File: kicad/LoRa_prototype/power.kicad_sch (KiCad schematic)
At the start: 56 parts, among them J10 SYS, J15 SYS, J2 USB_C_Receptacle_PowerOnly_6P, J3 BAT, J5 FG, J7 BQ, U1 TC1262-33, U2 BQ24074RGTT, U3 MAX17048, U4 SPV1050

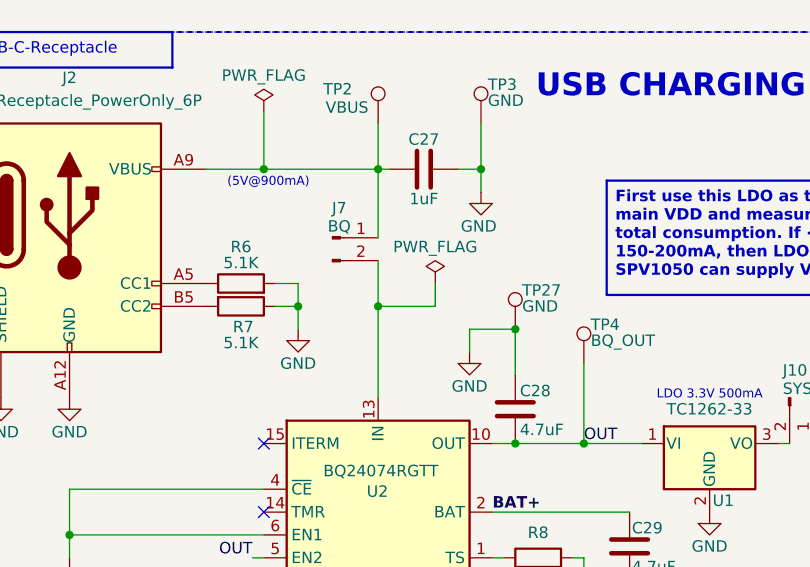
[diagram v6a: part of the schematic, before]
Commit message: Routed USB and charging IC
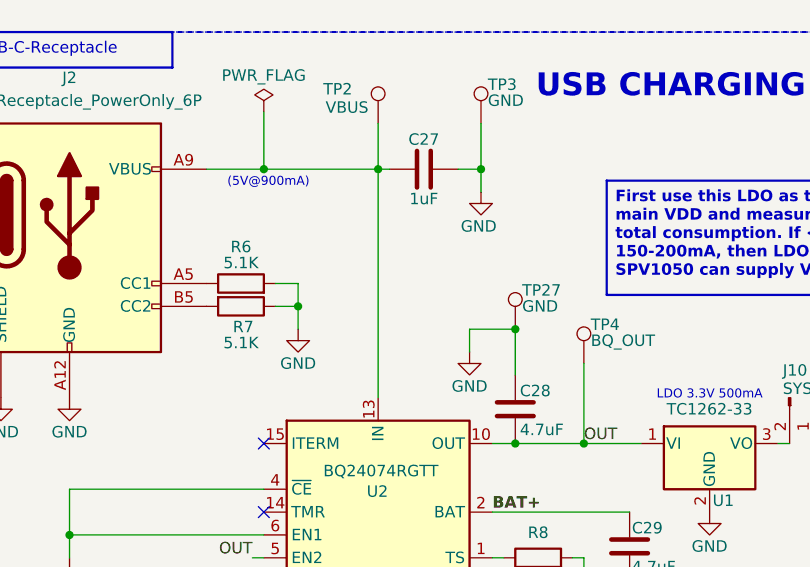
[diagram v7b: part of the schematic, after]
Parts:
- removed J7: BQ, Connector_PinHeader_2.54mm:PinHeader_1x02_P2.54mm_Vertical, symbol Connector:Conn_01x02_Pin
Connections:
- net at C27.1, J2.A9 (VBUS), J2.B9 (VBUS)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: now also U2.13 (IN)
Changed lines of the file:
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@@
 	)
 	(junction
-		(at 80.01 107.95)
-		(diameter 0)
-		(color 0 0 0 0)
-	)
-	(junction
 		(at 179.07 104.14)
 		(diameter 0)
@@
 	(wire
 		(pts
-			(xy 86.36 105.41) (xy 86.36 107.95)
-		)
-		(stroke
-			(width 0)
-			(type default)
-		)
-	)
-	(wire
-		(pts
 			(xy 128.27 123.19) (xy 133.35 123.19)
 		)
@@
 	(wire
 		(pts
-			(xy 86.36 107.95) (xy 80.01 107.95)
-		)
-		(stroke
-			(width 0)
-			(type default)
-		)
-	)
-	(wire
-		(pts
-			(xy 80.01 107.95) (xy 80.01 118.11)
-		)
-		(stroke
-			(width 0)
-			(type default)
-		)
-	)
-	(wire
-		(pts
 			(xy 153.67 123.19) (xy 153.67 125.73)
 		)
@@
 	(wire
 		(pts
-			(xy 80.01 102.87) (xy 80.01 107.95)
+			(xy 80.01 92.71) (xy 80.01 118.11)
 		)
 		(stroke
@@
 	(wire
 		(pts
-			(xy 80.01 92.71) (xy 80.01 100.33)
-		)
-		(stroke
-			(width 0)
-			(type default)
-		)
-	)
-	(wire
-		(pts
 			(xy 219.71 29.21) (xy 219.71 33.02)
 		)
@@
 	)
 	(symbol
-		(lib_id "power:PWR_FLAG")
-		(at 86.36 105.41 0)
-		(unit 1)
-		(body_style 1)
-		(exclude_from_sim no)
-		(in_bom yes)
-		(on_board yes)
-		(in_pos_files yes)
-		(dnp no)
-		(property "Reference" "#FLG010"
-			(at 86.36 103.505 0)
-			(hide yes)
-			(show_name no)
-			(do_not_autoplace no)
-			(effects
-				(font
-					(size 1.27 1.27)
-				)
-			)
-		)
-		(property "Value" "PWR_FLAG"
-			(at 86.36 101.346 0)
-			(show_name no)
-			(do_not_autoplace no)
-			(effects
-				(font
-					(size 1.27 1.27)
-				)
-			)
-		)
-		(property "Footprint" ""
-			(at 86.36 105.41 0)
-			(hide yes)
-			(show_name no)
-			(do_not_autoplace no)
-			(effects
-				(font
-					(size 1.27 1.27)
-				)
-			)
-		)
-		(property "Datasheet" ""
-			(at 86.36 105.41 0)
-			(hide yes)
-			(show_name no)
-			(do_not_autoplace no)
-			(effects
-				(font
-					(size 1.27 1.27)
-				)
-			)
-		)
-		(property "Description" "Special symbol for telling ERC where power comes from"
-			(at 86.36 105.41 0)
-			(hide yes)
-			(show_name no)
-			(do_not_autoplace no)
-			(effects
-				(font
-					(size 1.27 1.27)
-				)
-			)
-		)
-		(pin "1"
-		)
-		(instances
-			(project "LoRa_prototype"
-				(path "/9fad4700-f514-47ad-821a-b4076ecc08de/5f290f36-0c09-4232-84b9-bfe06ad06aa2"
-					(reference "#FLG010")
-					(unit 1)
-				)
-			)
-		)
-	)
-	(symbol
 		(lib_id "Device:C")
 		(at 205.74 91.44 180)
@@
 	)
 	(symbol
-		(lib_id "Connector:Conn_01x02_Pin")
-		(at 74.93 100.33 0)
-		(unit 1)
-		(body_style 1)
-		(exclude_from_sim no)
-		(in_bom yes)
-		(on_board yes)
-		(in_pos_files yes)
-		(dnp no)
-		(property "Reference" "J7"
-			(at 75.692 97.028 0)
-			(show_name no)
-			(do_not_autoplace no)
-			(effects
-				(font
-					(size 1.27 1.27)
-				)
-			)
-		)
-		(property "Value" "BQ"
-			(at 75.692 99.06 0)
-			(show_name no)
-			(do_not_autoplace no)
-			(effects
-				(font
-					(size 1.27 1.27)
-				)
-			)
-		)
-		(property "Footprint" "Connector_PinHeader_2.54mm:PinHeader_1x02_P2.54mm_Vertical"
-			(at 74.93 100.33 0)
-			(hide yes)
-			(show_name no)
-			(do_not_autoplace no)
-			(effects
-				(font
-					(size 1.27 1.27)
-				)
-			)
-		)
-		(property "Datasheet" ""
-			(at 74.93 100.33 0)
-			(hide yes)
-			(show_name no)
-			(do_not_autoplace no)
-			(effects
-				(font
-					(size 1.27 1.27)
-				)
-			)
-		)
-		(property "Description" "Generic connector, single row, 01x02, script generated"
-			(at 74.93 100.33 0)
-			(hide yes)
-			(show_name no)
-			(do_not_autoplace no)
-			(effects
-				(font
-					(size 1.27 1.27)
-				)
-			)
-		)
-		(pin "1"
-		)
-		(pin "2"
-		)
-		(instances
-			(project "LoRa_prototype"
-				(path "/9fad4700-f514-47ad-821a-b4076ecc08de/5f290f36-0c09-4232-84b9-bfe06ad06aa2"
-					(reference "J7")
-					(unit 1)
-				)
-			)
-		)
-	)
-	(symbol
 		(lib_id "power:GND")
 		(at 171.45 46.99 0)
@@
 			"15892596-2a56-42f9-87bc-d63facef6128" "15e0629a-49a6-4d89-a801-d5b90bb61a09"
 			"1606b332-549d-4356-ac60-6c5b5853a274" "17470208-3fc8-45d2-9301-407141016e98"
-			"19335232-9d4d-4c08-8b45-cce991ae32a1" "19df826f-f66b-4fd8-8010-44a60ef02bc0"
-			"1e86c9a5-56a8-443a-a601-b7e121ba0560" "2ac1fa60-a83a-486d-8e9b-da9936917350"
-			"2afca3db-305f-4098-a72a-d75c0786e537" "2c062ef6-a26b-45d0-8f0c-54ed535667b8"
-			"2f6ee398-578c-4367-b463-9ac0528bcf5e" "313899bc-2ad0-430e-8220-9b4901628631"
-			"36e6f0b5-4463-4bbd-a5eb-ef140118b323" "375cd1dd-6071-460e-b853-b380b78d5270"
+			"19df826f-f66b-4fd8-8010-44a60ef02bc0" "1e86c9a5-56a8-443a-a601-b7e121ba0560"
+			"2ac1fa60-a83a-486d-8e9b-da9936917350" "2afca3db-305f-4098-a72a-d75c0786e537"
+			"2c062ef6-a26b-45d0-8f0c-54ed535667b8" "2f6ee398-578c-4367-b463-9ac0528bcf5e"
+			"313899bc-2ad0-430e-8220-9b4901628631" "375cd1dd-6071-460e-b853-b380b78d5270"
 			"3869c621-7daa-4418-8ebe-a4226664ba23" "3b55cd7b-7118-4a57-bd28-a414f04beafe"
 			"3b7a4b9a-dfea-4b2d-ba0f-ee9f8ddfd35f" "3b7d618b-25e5-4183-ac75-f4e0437d3862"
@@
 			"6445f31d-8eb7-40e8-bbb4-238bfed47718" "66c26107-e4c7-45bf-802c-2413609b436a"
 			"6ac0af04-d7a4-4950-bed7-f84b7f1c962d" "6afd0259-80ed-4b22-b43b-e3c8370e289e"
-			"6c4368cd-6a92-4c4c-9005-fe4d29829b70" "6d50a834-2d9b-4ec7-a673-4275efa85f1e"
-			"6e0891ad-1c62-48af-ac2e-4c1d928da482" "6eb8ca3a-7038-41fb-86b1-b4cb45f65892"
+			"6c4368cd-6a92-4c4c-9005-fe4d29829b70" "6eb8ca3a-7038-41fb-86b1-b4cb45f65892"
 			"7542a80e-1430-4bb9-bab3-85b6fe3095be" "7620715f-3375-4a3d-9441-7319932c6382"
 			"76b839ee-4e0f-444f-a1be-78e2430f7b36" "76c65e56-74f1-40f5-a7bf-41e078eadd54"
@@
 			"868a5829-1a6e-4a2a-acea-dc354bd9375e" "87b47428-485f-49f1-9e98-f1a5620a7f27"
 			"895f76b3-dfa7-474a-915b-7c14e7be5d31" "8a08cdc5-0da8-4fb2-b7dc-b38bb792e6a4"
-			"8ad8f97c-d121-49ae-a8eb-66ee61dc3e9b" "8d3841c9-e323-424e-967d-74f4c5c6f9ac"
-			"8eb2b09e-806c-4948-b1b2-e00f1869fe03" "91c81378-1589-432e-85fc-fd990777d213"
-			"92461dfe-7dc1-459a-8e09-c0f3ef9803b2" "94471df4-0c86-4a05-b588-ea002a67924d"
-			"9541b335-7832-4153-ad49-c45b8932b985" "97965d07-c9ec-43be-8c8f-e2033080df90"
-			"9a329e44-bfa3-4818-8812-29979b08276b" "9de5a1e5-ee28-402d-9dd7-2d45dc0d8024"
-			"a8614e4f-d325-494f-af6e-e0da983fd2ea" "aa2cba69-aec2-4bc9-9406-a6f3da0db1fe"
-			"ae3053b4-115e-4b76-81b0-fbaeb94f27db" "b336cc52-ea98-402f-853d-335fef28a859"
-			"b39546db-1915-49ef-9aac-c7958663adae" "b98d5f9d-7db8-43d9-8e62-da5b473400b5"
-			"bd0d8184-9210-4ccf-b78c-09f32b56abc3" "be3c6c0a-f50d-4a35-b392-eb562d24de30"
-			"c219d99f-51ff-4033-bd79-8b2f6d5ff907" "c369d34f-0279-43f7-8e62-d515ee5e137c"
-			"c38673ba-d9f6-472a-a589-ec366962bbc1" "c523b646-58af-4ac2-b96d-eb1f52ed2117"
-			"c73048a0-de71-4700-a146-66fbedba28af" "c769fe5f-971b-4b6e-95b5-3d3dc5ee5efa"
-			"cebeb1c7-5dbe-401b-a2cf-d487a8f177ad" "d1fda7c0-454d-49d3-b614-9e0d56f116ff"
+			"8ad8f97c-d121-49ae-a8eb-66ee61dc3e9b" "8eb2b09e-806c-4948-b1b2-e00f1869fe03"
+			"91c81378-1589-432e-85fc-fd990777d213" "92461dfe-7dc1-459a-8e09-c0f3ef9803b2"
+			"94471df4-0c86-4a05-b588-ea002a67924d" "9541b335-7832-4153-ad49-c45b8932b985"
+			"97965d07-c9ec-43be-8c8f-e2033080df90" "9a329e44-bfa3-4818-8812-29979b08276b"
+			"9de5a1e5-ee28-402d-9dd7-2d45dc0d8024" "a8614e4f-d325-494f-af6e-e0da983fd2ea"
+			"aa2cba69-aec2-4bc9-9406-a6f3da0db1fe" "ae3053b4-115e-4b76-81b0-fbaeb94f27db"
+			"b336cc52-ea98-402f-853d-335fef28a859" "b39546db-1915-49ef-9aac-c7958663adae"
+			"b98d5f9d-7db8-43d9-8e62-da5b473400b5" "bd0d8184-9210-4ccf-b78c-09f32b56abc3"
+			"be3c6c0a-f50d-4a35-b392-eb562d24de30" "c219d99f-51ff-4033-bd79-8b2f6d5ff907"
+			"c369d34f-0279-43f7-8e62-d515ee5e137c" "c38673ba-d9f6-472a-a589-ec366962bbc1"
+			"c523b646-58af-4ac2-b96d-eb1f52ed2117" "c73048a0-de71-4700-a146-66fbedba28af"
+			"c769fe5f-971b-4b6e-95b5-3d3dc5ee5efa" "d1fda7c0-454d-49d3-b614-9e0d56f116ff"
 			"d6f28cbb-6360-4f1c-83dc-4e461ab27154" "d9cbc6dc-f403-4a5e-b66f-e6647fd9c796"
 			"dc3e67fe-721c-4dfd-be6d-d15449b3e772" "dcdd15e4-8fcb-4eb8-b2e1-62857ae4dece"
 			"e30c373b-a4d6-4257-84f3-d39e5cda2d30" "e3d2cb0b-7666-440e-bb43-34a346acf2d3"
-			"e432126c-771a-4696-b865-61fe22cde44f" "e4fc5512-e473-4f3c-a370-db67866444e2"
-			"e89ab80b-d04d-4dd5-a74e-e66792c26431" "ea2631b9-d313-4bcb-99d5-0f3f7e98a5ca"
-			"eb7ab00c-10d9-4953-8834-33fb20c0eefb" "f3bf8ef2-4591-4590-bcc4-122cb2412a2f"
-			"f3c84562-ee03-4509-ba8b-3518a36ea5cf" "f7a09951-235a-407c-a18a-952f9c38c4d9"
-			"fbce87b8-7507-4f0d-b9b1-3d1e4709bbe9"
+			"e4fc5512-e473-4f3c-a370-db67866444e2" "e89ab80b-d04d-4dd5-a74e-e66792c26431"
+			"ea2631b9-d313-4bcb-99d5-0f3f7e98a5ca" "eb7ab00c-10d9-4953-8834-33fb20c0eefb"
+			"f3bf8ef2-4591-4590-bcc4-122cb2412a2f" "f3c84562-ee03-4509-ba8b-3518a36ea5cf"
+			"f7a09951-235a-407c-a18a-952f9c38c4d9" "fbce87b8-7507-4f0d-b9b1-3d1e4709bbe9"
 		)
 	)

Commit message: Stable commit
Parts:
- removed TP29: SDA_FG, TestPoint:TestPoint_Pad_2.0x2.0mm, symbol Connector:TestPoint
- removed TP30: SCL_FG, TestPoint:TestPoint_Pad_2.0x2.0mm, symbol Connector:TestPoint
- removed TP6: ~{BAT_CHG}, TestPoint:TestPoint_Pad_2.0x2.0mm, symbol Connector:TestPoint
- removed TP7: ~{BAT_CONN}, TestPoint:TestPoint_Pad_2.0x2.0mm, symbol Connector:TestPoint
